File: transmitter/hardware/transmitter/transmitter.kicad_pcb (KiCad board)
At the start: 2 copper layers, 18 parts, among them J1 SOIL, J2 Conn_01x05, SW1 SW_SPST, SW2 SW_SPST, U1 NodeMCU_1.0_(ESP-12E), U2 MCP1700-3302E_SOT89, U3 CD4051B

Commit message: Layout
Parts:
- removed J2: Conn_01x05, Connector_PinHeader_2.54mm:PinHeader_1x05_P2.54mm_Vertical
- removed SW2: SW_SPST, Connector_PinHeader_2.54mm:PinHeader_1x02_P2.54mm_Vertical
- added J3: USB_UART_OFF, Connector_PinHeader_2.54mm:PinHeader_1x01_P2.54mm_Vertical, F.Cu at (167.6, 94.5)
- added J4: USB_UART_ON, Connector_PinHeader_2.54mm:PinHeader_1x01_P2.54mm_Vertical, F.Cu at (167.6, 92.0)
- TH1: moved to B.Cu
- moved R5 25.3 mm to (160.0, 71.1), turned to 270 degrees
- moved TH1 25.3 mm to (160.0, 73.7), turned to 180 degrees
- moved R4 24.2 mm to (158.8, 78.7), turned to 0 degrees
- moved J1 21.6 mm to (156.2, 76.2)
- moved R3 21.6 mm to (156.2, 73.7), turned to 270 degrees
- moved BT1 12.5 mm to (129.5, 97.1), turned to 180 degrees
- moved C2 11.7 mm to (145.0, 68.0)
- moved C3 10.4 mm to (148.6, 104.1)
- moved R1 10.2 mm to (157.5, 95.2)
- moved R2 10.2 mm to (157.5, 97.3)
- moved U2 9.66 mm to (148.6, 99.1)
- moved C4 9.55 mm to (148.6, 95.2)
- moved SW1 7.73 mm to (167.6, 81.3)
- moved U3 5.24 mm to (144.8, 71.1)
- moved C1 4.75 mm to (152.0, 68.0)
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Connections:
- U1 pad 10: Net-(U1-Pad10) -> (no net)
- U1 pad 12: Net-(U1-Pad12) -> (no net)
- U1 pad 15: /USB_UART_PWR -> (no net)
- U1 pad 16: Net-(U1-Pad16) -> (no net)
- U1 pad 17: Net-(U1-Pad17) -> (no net)
- U1 pad 18: Net-(U1-Pad18) -> (no net)
- U1 pad 19: Net-(U1-Pad19) -> (no net)
- U1 pad 2: Net-(U1-Pad2) -> (no net)
- U1 pad 20: Net-(U1-Pad20) -> (no net)
- U1 pad 24: Net-(U1-Pad24) -> (no net)
- U1 pad 25: Net-(U1-Pad25) -> (no net)
- U1 pad 26: Net-(U1-Pad26) -> (no net)
- U1 pad 27: Net-(U1-Pad27) -> (no net)
- U1 pad 28: Net-(U1-Pad28) -> (no net)
- U1 pad 3: Net-(U1-Pad3) -> (no net)
- U1 pad 4: Net-(U1-Pad4) -> (no net)
- U1 pad 5: Net-(U1-Pad5) -> (no net)
- U1 pad 6: Net-(U1-Pad6) -> (no net)
- U1 pad 7: Net-(U1-Pad7) -> (no net)
- U1 pad 8: Net-(U1-Pad8) -> (no net)
- U1 pad 9: Net-(U1-Pad9) -> (no net)
- U3 pad 1: Net-(J2-Pad2) -> (no net)
- U3 pad 12: Net-(J2-Pad1) -> (no net)
- U3 pad 2: Net-(J2-Pad4) -> (no net)
- U3 pad 4: Net-(J2-Pad5) -> (no net)
- U3 pad 5: Net-(J2-Pad3) -> (no net)
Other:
- board outline added: 43 x 42 mm

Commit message: All connected
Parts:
- moved C2 10.2 mm to (155.1, 68.9), turned to 90 degrees
- moved SW1 5.72 mm to (167.6, 75.6), turned to 0 degrees
- moved R1 5.19 mm to (153.8, 98.9)
- moved R2 5.00 mm to (153.8, 100.7)
- moved TH1 4.02 mm to (156.2, 72.4), turned to 270 degrees
- moved J4 3.91 mm to (167.6, 95.9)
- moved R5 3.06 mm to (157.9, 68.9), turned to 90 degrees
- moved R4 2.84 mm to (156.2, 80.0), turned to 180 degrees
- moved U3 1.91 mm to (144.8, 73.0)
- moved C3 1.30 mm to (148.5, 102.8)
- moved R3 1.27 mm to (156.2, 74.9), turned to 0 degrees
- moved J1 1.27 mm to (156.2, 77.5), turned to 90 degrees
- moved J3 1.17 mm to (167.6, 93.3)
- moved C1 1.01 mm to (152.4, 68.9), turned to 90 degrees
- moved U2 0.26 mm to (148.8, 98.9), turned to 180 degrees
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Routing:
- net GND: track 0.00 -> 175.1 mm
- net RESET: track 0.00 -> 74.4 mm
- net 3V3: track 0.00 -> 47.6 mm, vias 0 -> 1
- net /BATT: track 0.00 -> 36.2 mm
- net BATT_SENSE: track 0.00 -> 23.5 mm
- net SENSE_PWR: track 0.00 -> 19.3 mm
- net A0: track 0.00 -> 14.4 mm
- net TEMP_SENSE: track 0.00 -> 12.5 mm, vias 0 -> 1
- net Net-(SW1-Pad2): track 0.00 -> 12.3 mm
- net Net-(U1-Pad23): track 0.00 -> 10.2 mm
- net Net-(U1-Pad22): track 0.00 -> 10.2 mm
- net Net-(U1-Pad21): track 0.00 -> 10.2 mm
- net SOIL_SENSE: track 0.00 -> 6.98 mm
- net Net-(J1-Pad2): track 0.00 -> 3.23 mm
- added copper zone on B.Cu, net GND
- added copper zone on F.Cu, net GND

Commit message: Power traces
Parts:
- J1: moved to B.Cu
- turned J1 to 270 degrees
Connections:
- U1 pad 10: (no net) -> GND
- U1 pad 16: (no net) -> 3V3
- U1 pad 17: (no net) -> GND
- U1 pad 24: (no net) -> GND
- U1 pad 25: (no net) -> 3V3
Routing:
- net GND: track 175.1 -> 157.3 mm
- net 3V3: track 47.6 -> 63.9 mm
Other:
- board size 43 x 42 mm -> 42 x 42 mm
- net class BATT added: clearance 0.25, trace_width 0.5, via_dia 0.8, via_drill 0.4

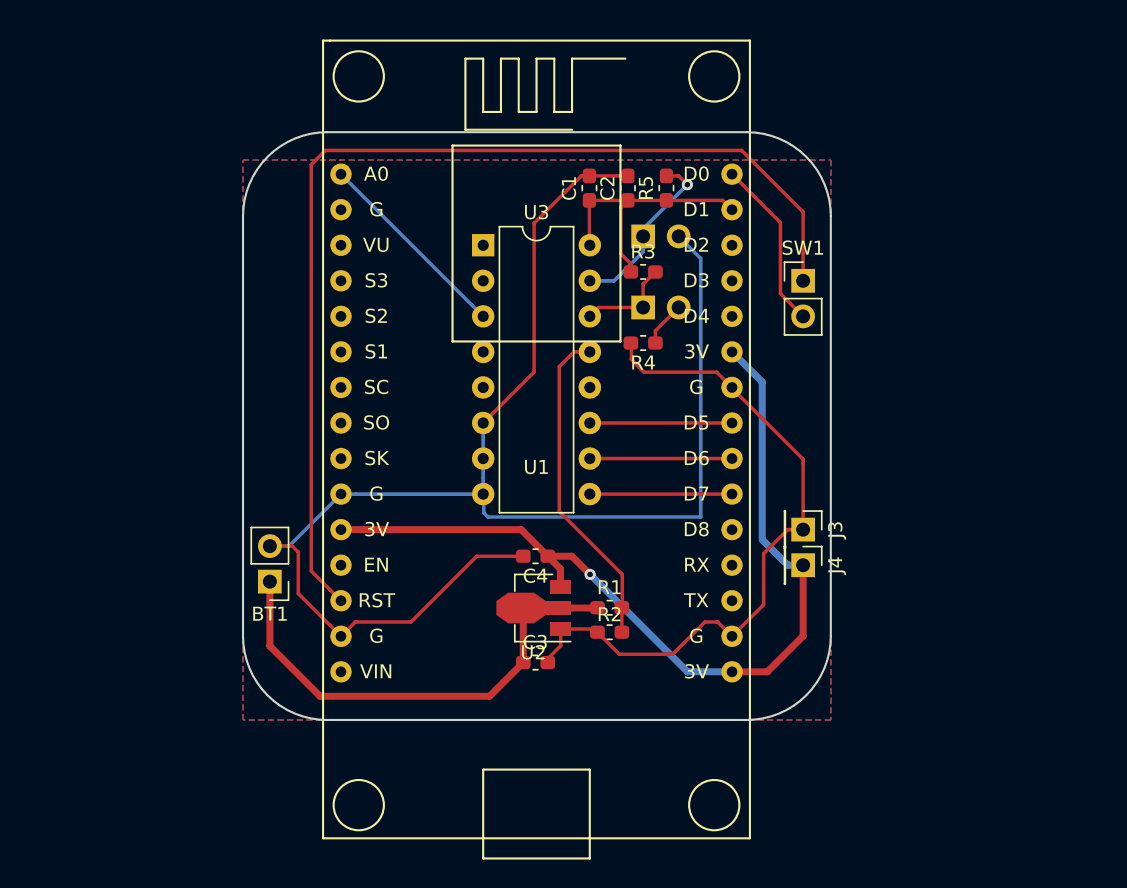
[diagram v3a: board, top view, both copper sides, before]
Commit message: JST connectors
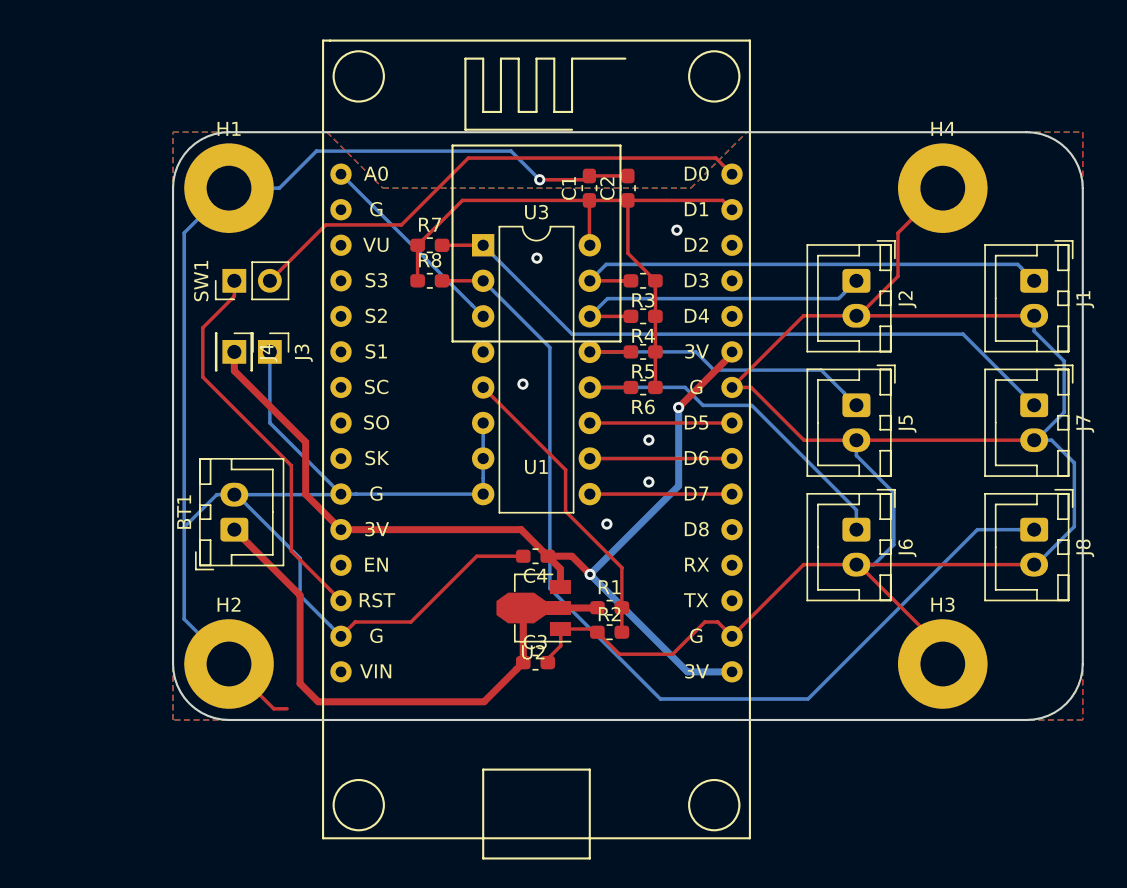
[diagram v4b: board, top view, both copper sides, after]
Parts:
- removed TH1: Thermistor, Connector_PinHeader_2.54mm:PinHeader_1x02_P2.54mm_Vertical
- added H1: MountingHole, MountingHole:MountingHole_3.2mm_M3_Pad, F.Cu at (126.6, 68.9)
- added H2: MountingHole, MountingHole:MountingHole_3.2mm_M3_Pad, F.Cu at (126.6, 102.9)
- added H3: MountingHole, MountingHole:MountingHole_3.2mm_M3_Pad, F.Cu at (177.6, 102.9)
- added H4: MountingHole, MountingHole:MountingHole_3.2mm_M3_Pad, F.Cu at (177.6, 68.9)
- added J2: SOIL, Connector_JST:JST_XH_B02B-XH-A_1x02_P2.50mm_Vertical, F.Cu at (171.4, 75.6)
- added J5: SOIL, Connector_JST:JST_XH_B02B-XH-A_1x02_P2.50mm_Vertical, F.Cu at (171.4, 84.5)
- added J6: SOIL, Connector_JST:JST_XH_B02B-XH-A_1x02_P2.50mm_Vertical, F.Cu at (171.4, 93.3)
- added J7: SOIL, Connector_JST:JST_XH_B02B-XH-A_1x02_P2.50mm_Vertical, F.Cu at (184.2, 84.5)
- added J8: SOIL, Connector_JST:JST_XH_B02B-XH-A_1x02_P2.50mm_Vertical, F.Cu at (184.2, 93.3)
- added R6: 10K, Resistor_SMD:R_0603_1608Metric_Pad1.05x0.95mm_HandSolder, F.Cu at (156.2, 83.2)
- added R7: 10K, Resistor_SMD:R_0603_1608Metric_Pad1.05x0.95mm_HandSolder, F.Cu at (141.0, 73.0)
- added R8: 10K, Resistor_SMD:R_0603_1608Metric_Pad1.05x0.95mm_HandSolder, F.Cu at (141.0, 75.6)
- BT1: footprint Connector_PinHeader_2.54mm:PinHeader_1x02_P2.54mm_Vertical -> Connector_JST:JST_XH_B02B-XH-A_1x02_P2.50mm_Vertical
- J1: footprint Connector_PinHeader_2.54mm:PinHeader_1x02_P2.54mm_Vertical -> Connector_JST:JST_XH_B02B-XH-A_1x02_P2.50mm_Vertical; moved to F.Cu
- R4: value 1K -> 10K
- moved J4 43.4 mm to (127.0, 80.6)
- moved SW1 40.6 mm to (127.0, 75.6), turned to 90 degrees
- moved J3 40.2 mm to (129.5, 80.6)
- moved J1 28.0 mm to (184.2, 75.6)
- moved R5 11.8 mm to (156.2, 80.6), turned to 180 degrees
- moved BT1 4.50 mm to (127.0, 93.3), turned to 90 degrees
- moved R4 1.91 mm to (156.2, 78.1)
- moved R3 0.63 mm to (156.2, 75.6), turned to 180 degrees
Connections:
- J1 pad 1: SOIL_SENSE -> SOIL_1
- J1 pad 2: Net-(J1-Pad2) -> GND
- R3 pad 2: SOIL_SENSE -> SOIL_1
- R4 pad 1: Net-(J1-Pad2) -> SENSE_PWR
- R4 pad 2: GND -> SOIL_2
- R5 pad 2: TEMP_SENSE -> SOIL_3
- U3 pad 1: (no net) -> SOIL_5
- U3 pad 12: (no net) -> SOIL_4
- U3 pad 13: BATT_SENSE -> SOIL_3
- U3 pad 14: SOIL_SENSE -> SOIL_2
- U3 pad 15: TEMP_SENSE -> SOIL_1
- U3 pad 2: (no net) -> SOIL_6
- U3 pad 5: (no net) -> BATT_SENSE
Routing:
- net GND: track 157.3 -> 285.1 mm, vias 0 -> 7
- net SOIL_6: track 0.00 -> 69.8 mm
- net SOIL_5: track 0.00 -> 47.0 mm
- net RESET: track 74.4 -> 27.9 mm
- net SOIL_1: track 0.00 -> 35.7 mm
- net SOIL_4: track 0.00 -> 27.0 mm
- net Net-(SW1-Pad2): track 12.3 -> 37.1 mm
- net SENSE_PWR: track 19.3 -> 44.0 mm
- net SOIL_3: track 0.00 -> 23.6 mm
- net SOIL_2: track 0.00 -> 23.0 mm
- net TEMP_SENSE: track 12.5 -> 0.00 mm, vias 1 -> 0
- net SOIL_SENSE: track 6.98 -> 0.00 mm
- net 3V3: track 63.9 -> 70.7 mm, vias 1 -> 2
- net /BATT: track 36.0 -> 41.4 mm
- net Net-(J1-Pad2): track 3.23 -> 0.00 mm
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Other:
- board size 42 x 42 mm -> 65 x 42 mm

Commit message: Vin & battery straps
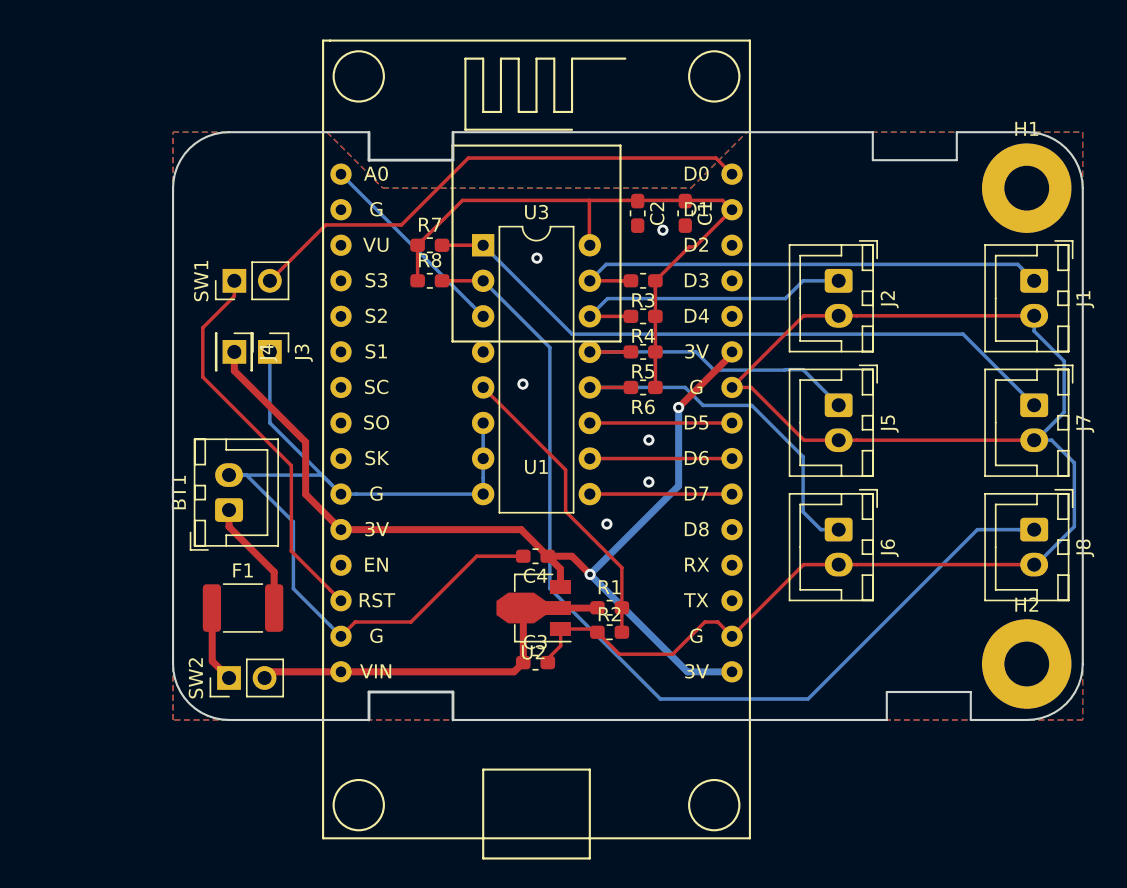
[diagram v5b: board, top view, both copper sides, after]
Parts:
- removed H3, H4: MountingHole, MountingHole:MountingHole_3.2mm_M3_Pad
- added F1: Polyfuse, Fuse:Fuse_1812_4532Metric_Pad1.30x3.40mm_HandSolder, F.Cu at (127.6, 98.9)
- added SW2: SW, Connector_PinHeader_2.54mm:PinHeader_1x02_P2.54mm_Vertical, F.Cu at (126.6, 103.9)
- moved H1 57.0 mm to (183.6, 68.9)
- moved H2 57.0 mm to (183.6, 102.9)
- moved C1 7.08 mm to (159.2, 70.7), turned to 270 degrees
- moved C2 1.93 mm to (155.8, 70.7), turned to 270 degrees
- moved BT1 1.45 mm to (126.6, 91.9)
- moved J2 1.27 mm to (170.2, 75.6)
- moved J5 1.27 mm to (170.2, 84.5)
- moved J6 1.27 mm to (170.2, 93.3)
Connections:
- BT1 pad 1: /BATT -> Net-(BT1-Pad1)
- U1 pad 15: (no net) -> /BATT
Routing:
- net GND: track 285.1 -> 177.7 mm, vias 7 -> 6
- net /BATT: track 41.4 -> 29.7 mm
- net Net-(BT1-Pad1): track 0.00 -> 8.34 mm
- net Net-(F1-Pad1): track 0.00 -> 5.51 mm
- net SOIL_2: track 23.0 -> 21.8 mm
- net SOIL_3: track 23.6 -> 22.3 mm
- net SENSE_PWR: track 44.0 -> 45.0 mm
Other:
- outline, holes or cut-outs redrawn
- board text added: "Battery"

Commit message: battery straps
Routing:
- net /BATT: track 29.7 -> 31.2 mm
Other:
- outline, holes or cut-outs redrawn
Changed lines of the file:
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@@
     (thickness 1.6)
     (drawings 28)
-    (tracks 171)
+    (tracks 173)
     (zones 0)
     (modules 29)
@@
   )
   (gr_line (start 179.62 106.945) (end 183.62 106.945) (layer Edge.Cuts) (width 0.15))
-  (gr_line (start 178.62 64.945) (end 183.62 64.945) (layer Edge.Cuts) (width 0.15))
-  (gr_line (start 178.62 66.945) (end 178.62 64.945) (layer Edge.Cuts) (width 0.15))
-  (gr_line (start 172.62 66.945) (end 178.62 66.945) (layer Edge.Cuts) (width 0.15))
-  (gr_line (start 172.62 64.945) (end 172.62 66.945) (layer Edge.Cuts) (width 0.15))
+  (gr_line (start 179.62 64.945) (end 183.62 64.945) (layer Edge.Cuts) (width 0.15))
+  (gr_line (start 179.62 66.945) (end 179.62 64.945) (layer Edge.Cuts) (width 0.15))
+  (gr_line (start 173.62 66.945) (end 179.62 66.945) (layer Edge.Cuts) (width 0.15))
+  (gr_line (start 173.62 64.945) (end 173.62 66.945) (layer Edge.Cuts) (width 0.15))
   (gr_line (start 179.62 104.945) (end 179.62 106.945) (layer Edge.Cuts) (width 0.15))
   (gr_line (start 173.62 104.945) (end 179.62 104.945) (layer Edge.Cuts) (width 0.15))
@@
   (gr_line (start 173.62 106.945) (end 142.62 106.945) (layer Edge.Cuts) (width 0.15))
   (gr_line (start 187.62 68.945) (end 187.62 102.945) (layer Edge.Cuts) (width 0.15))
-  (gr_line (start 142.62 64.945) (end 172.62 64.945) (layer Edge.Cuts) (width 0.15))
+  (gr_line (start 142.62 64.945) (end 173.62 64.945) (layer Edge.Cuts) (width 0.15))
   (segment (start 147.645 99.1035) (end 147.4865 98.945) (width 0.5) (layer F.Cu) (net 1) (status 30))
   (segment (start 147.645 102.845) (end 147.645 99.1035) (width 0.5) (layer F.Cu) (net 1) (status 30))
@@
   (segment (start 147.4865 98.945) (end 152.92 98.945) (width 0.5) (layer F.Cu) (net 1) (status 30))
   (segment (start 147.4865 98.945) (end 146.153 98.945) (width 0.5) (layer F.Cu) (net 1) (status 30))
-  (segment (start 146.985 103.505) (end 147.645 102.845) (width 0.5) (layer F.Cu) (net 1))
-  (segment (start 134.62 103.505) (end 146.985 103.505) (width 0.5) (layer F.Cu) (net 1))
   (segment (start 129.6 103.505) (end 129.16 103.945) (width 0.5) (layer F.Cu) (net 1))
   (segment (start 134.62 103.505) (end 129.6 103.505) (width 0.5) (layer F.Cu) (net 1))
+  (segment (start 140.821999 102.743001) (end 144.62 98.945) (width 0.5) (layer F.Cu) (net 1))
+  (segment (start 144.62 98.945) (end 147.4865 98.945) (width 0.5) (layer F.Cu) (net 1))
+  (segment (start 135.381999 102.743001) (end 140.821999 102.743001) (width 0.5) (layer F.Cu) (net 1))
+  (segment (start 134.62 103.505) (end 135.381999 102.743001) (width 0.5) (layer F.Cu) (net 1))
   (segment (start 152.71 100.445) (end 152.94 100.675) (width 0.25) (layer F.Cu) (net 2) (status 30))
   (segment (start 150.3 100.445) (end 152.71 100.445) (width 0.25) (layer F.Cu) (net 2) (status 30))

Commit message: TP4056
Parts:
- removed BT1: Battery, Connector_JST:JST_XH_B02B-XH-A_1x02_P2.50mm_Vertical
- removed H1, H2: MountingHole, MountingHole:MountingHole_3.2mm_M3_Pad
- J3: value USB_UART_OFF -> USB_UART; footprint Connector_PinHeader_2.54mm:PinHeader_1x01_P2.54mm_Vertical -> Connector_PinHeader_2.54mm:PinHeader_1x02_P2.54mm_Vertical
- J4: value USB_UART_ON -> PWR; footprint Connector_PinHeader_2.54mm:PinHeader_1x01_P2.54mm_Vertical -> tp4056:tp4056
- moved SW1 26.8 mm to (129.5, 102.2), turned to 180 degrees
- moved J7 19.8 mm to (170.2, 98.4)
- moved J8 18.9 mm to (170.2, 106.0)
- moved J1 15.9 mm to (170.2, 67.9)
- moved J3 15.5 mm to (127.0, 95.9), turned to 90 degrees
- moved J4 14.7 mm to (115.6, 89.9), turned to 90 degrees
- moved F1 8.19 mm to (124.1, 106.3), turned to 90 degrees
- moved SW2 5.47 mm to (129.5, 108.6), turned to 180 degrees
- moved J6 2.54 mm to (170.2, 90.8)
- moved J5 1.27 mm to (170.2, 83.2)
- moved C1 0.72 mm to (159.4, 71.4)
- moved C2 0.70 mm to (155.9, 71.4)
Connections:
- net /BATT renamed /PWR
- F1 pad 2: Net-(BT1-Pad1) -> /OUT+
- J4 pad 1: 3V3 -> GND
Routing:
- net GND: track 177.7 -> 82.2 mm, vias 6 -> 7
- net Net-(SW1-Pad2): track 37.1 -> 73.1 mm
- net /OUT+: track 0.00 -> 23.2 mm
- net RESET: track 27.9 -> 6.66 mm
- net SOIL_6: track 69.8 -> 52.2 mm
- net SOIL_1: track 35.7 -> 23.9 mm
- net SOIL_5: track 47.0 -> 58.7 mm
- net 3V3: track 70.7 -> 61.0 mm
- net Net-(BT1-Pad1): track 8.34 -> 0.00 mm
- net SOIL_4: track 27.2 -> 23.9 mm
- net SENSE_PWR: track 45.0 -> 43.6 mm
- net SOIL_3: track 22.3 -> 21.8 mm
- net /PWR: track 31.2 -> 31.7 mm
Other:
- board size 65 x 42 mm -> 61 x 47 mm
- board text added: "TP4056"

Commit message: Labels
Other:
- board text added: "3V3"
- board text added: "GND"
- board text added: "OUT+"
- board text added: "OUT-"
- board text added: "POWER"
- board text added: "SLEEP"
- board text added: "SOIL 1"
- board text added: "SOIL 2"
- board text added: "SOIL 3"
- board text added: "SOIL 4"
- board text added: "SOIL 5"
- board text added: "SOIL 6"
